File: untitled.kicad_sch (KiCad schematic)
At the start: 12 parts, among them J2 LED HDR, U1 74LVC2GU04

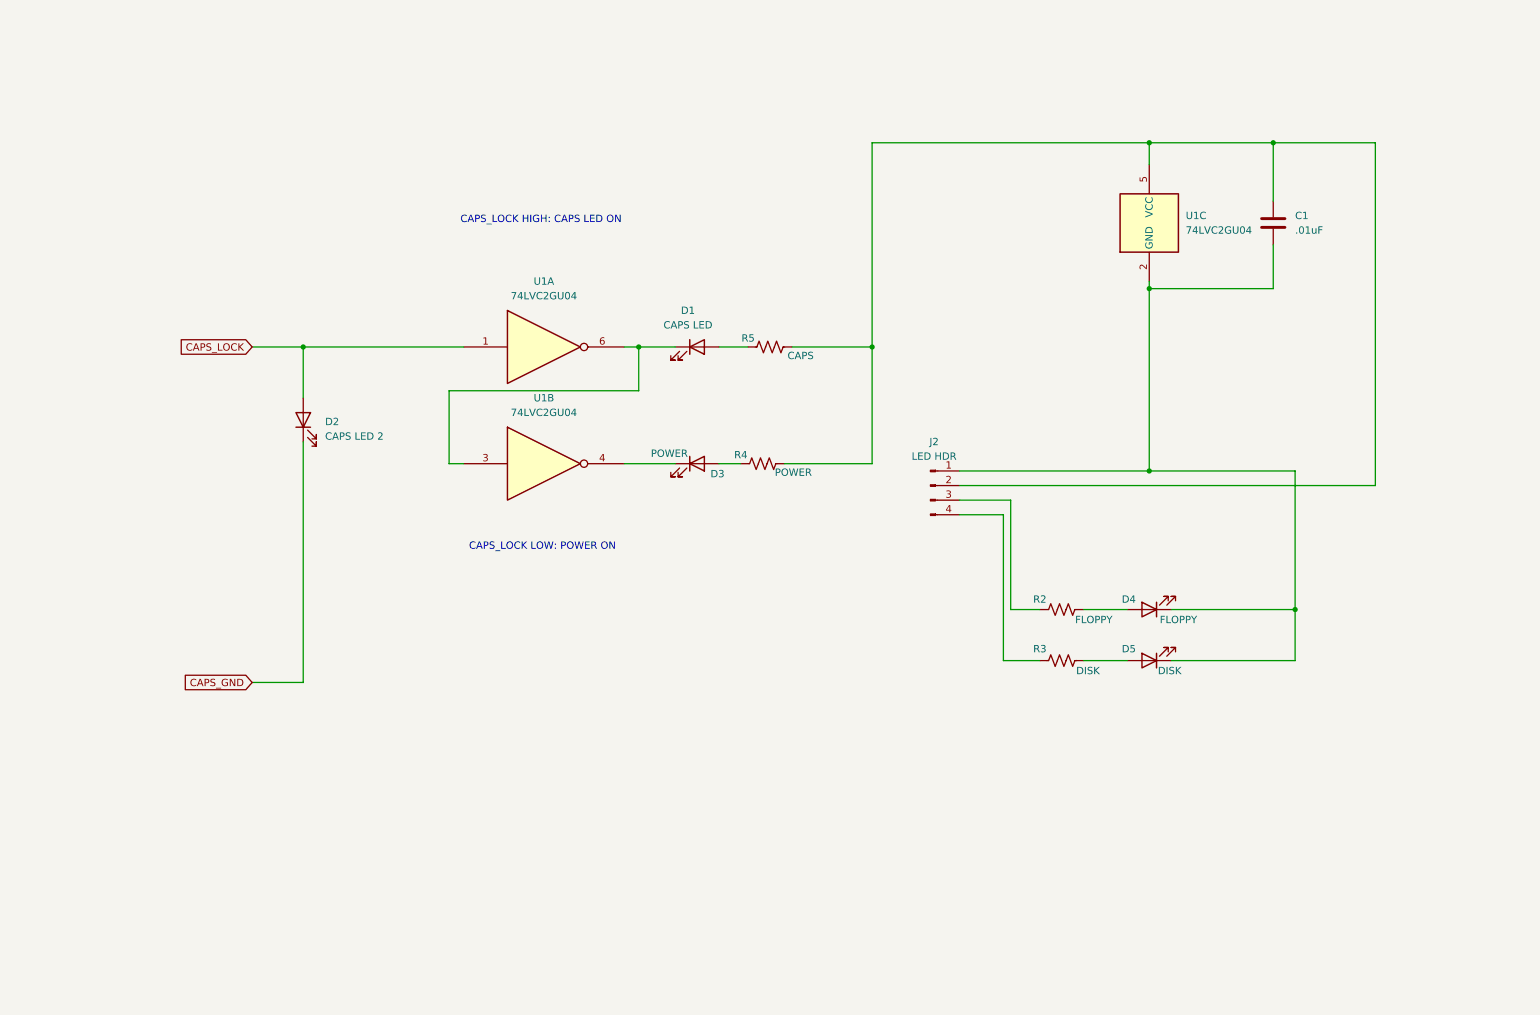
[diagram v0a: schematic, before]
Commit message: r2
smaller cutouts for stabilizers in PCB
removed unused mounting holes
board shorter by 2mm top/bottom to mount rails
add 0R option to use capslock under keycap only
silkscreen labels for switches
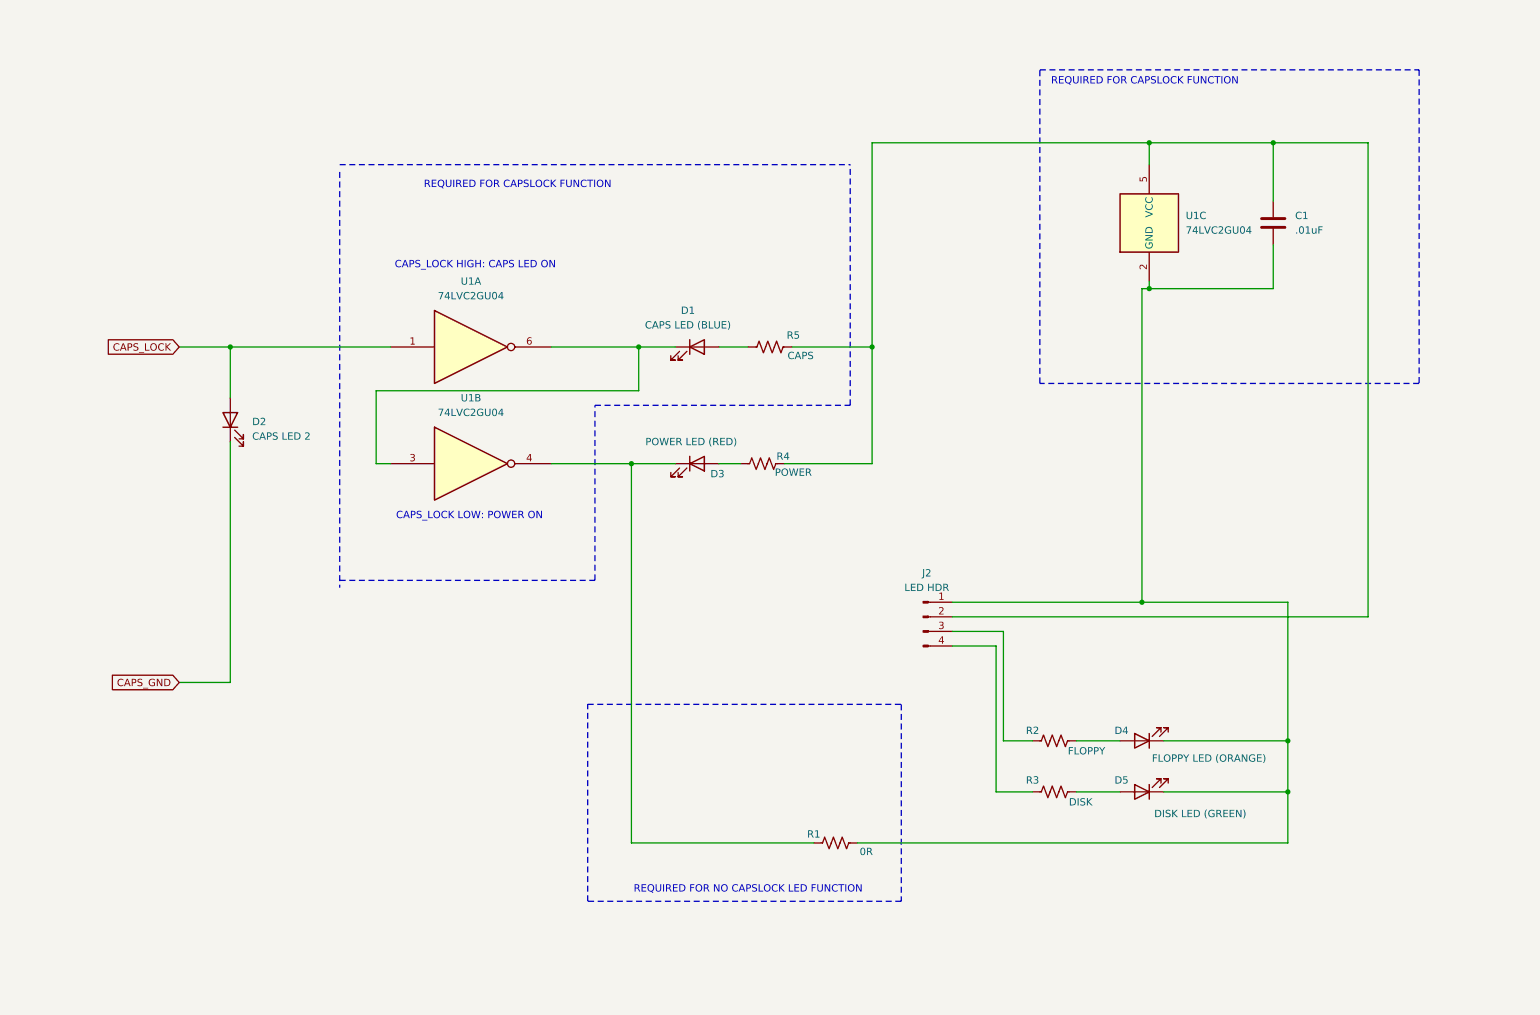
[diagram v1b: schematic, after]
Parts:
- added R1: 0R, Resistor_SMD:R_0805_2012Metric_Pad1.20x1.40mm_HandSolder, symbol Device:R_US
- D1: value CAPS LED -> CAPS LED (BLUE)
- D3: value POWER -> POWER LED (RED)
- D4: value FLOPPY -> FLOPPY LED (ORANGE)
- D5: value DISK -> DISK LED (GREEN)
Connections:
- net at C1.2, D4.1 (K), D5.1 (K)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: now also R1.2
- net at D3.1 (K), U1.4: now also R1.1
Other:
- note added: "REQUIRED FOR CAPSLOCK FUNCTION"
- note added: "REQUIRED FOR NO CAPSLOCK LED FUNCTION"
- moved on the sheet: D2, D4, D5, J2, R2, R3, U1A, U1B

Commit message: fab 9/7/24 KS-33 revised caps LED
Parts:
- D1: value CAPS LED (BLUE) -> POWER LED (RED)
- D3: value POWER LED (RED) -> CAPS LOCK (BLUE)
- R4: value POWER -> CAPS
- R5: value CAPS -> POWER
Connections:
- net CAPS_GND: now also U1.1
- net CAPS_LOCK renamed VCC
- net VCC: no longer U1.1
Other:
- moved on the sheet: D2
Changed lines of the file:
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@@
 	(paper "A4")
-	(junction
-		(at 53.34 73.66)
-		(diameter 0)
-		(color 0 0 0 0)
-	)
 	(junction
 		(at 124.46 73.66)
@@
 	)
 	(junction
+		(at 52.07 73.66)
+		(diameter 0)
+		(color 0 0 0 0)
+	)
+	(junction
 		(at 213.36 38.1)
 		(diameter 0)
@@
 	(wire
 		(pts
-			(xy 53.34 132.08) (xy 44.45 132.08)
-		)
-		(stroke
-			(width 0)
-			(type default)
-		)
-	)
-	(wire
-		(pts
-			(xy 53.34 73.66) (xy 53.34 82.55)
+			(xy 52.07 73.66) (xy 43.18 73.66)
+		)
+		(stroke
+			(width 0)
+			(type default)
+		)
+	)
+	(wire
+		(pts
+			(xy 52.07 41.91) (xy 52.07 50.8)
+		)
+		(stroke
+			(width 0)
+			(type default)
+		)
+	)
+	(wire
+		(pts
+			(xy 52.07 73.66) (xy 81.28 73.66)
 		)
 		(stroke
@@
 	(wire
 		(pts
-			(xy 53.34 73.66) (xy 81.28 73.66)
-		)
-		(stroke
-			(width 0)
-			(type default)
-		)
-	)
-	(wire
-		(pts
 			(xy 200.66 142.24) (xy 208.28 142.24)
 		)
@@
 	(wire
 		(pts
-			(xy 53.34 90.17) (xy 53.34 132.08)
+			(xy 52.07 58.42) (xy 52.07 73.66)
 		)
 		(stroke
@@
 	(wire
 		(pts
-			(xy 44.45 73.66) (xy 53.34 73.66)
+			(xy 43.18 41.91) (xy 52.07 41.91)
 		)
 		(stroke
@@
 		)
 	)
-	(global_label "CAPS_LOCK"
+	(global_label "VCC"
 		(shape input)
-		(at 44.45 73.66 180)
+		(at 43.18 41.91 180)
 		(fields_autoplaced yes)
 		(effects
@@
 		)
 		(property "Intersheetrefs" "${INTERSHEET_REFS}"
-			(at 30.7605 73.66 0)
+			(at 36.5662 41.91 0)
 			(effects
 				(font
@@
 	(global_label "CAPS_GND"
 		(shape input)
-		(at 44.45 132.08 180)
+		(at 43.18 73.66 180)
 		(fields_autoplaced yes)
 		(effects
@@
 		)
 		(property "Intersheetrefs" "${INTERSHEET_REFS}"
-			(at 31.7886 132.08 0)
+			(at 30.5186 73.66 0)
 			(effects
 				(font
@@
 	(symbol
 		(lib_id "Device:LED")
-		(at 53.34 86.36 90)
+		(at 52.07 54.61 90)
 		(unit 1)
 		(exclude_from_sim no)
@@
 		(fields_autoplaced yes)
 		(property "Reference" "D2"
-			(at 57.15 86.6774 90)
+			(at 55.88 54.9274 90)
 			(effects
 				(font
@@
 		)
 		(property "Value" "CAPS LED 2"
-			(at 57.15 89.2174 90)
+			(at 55.88 57.4674 90)
 			(effects
 				(font
@@
 		)
 		(property "Footprint" "LED_SMD:LED_0805_2012Metric"
-			(at 53.34 86.36 0)
+			(at 52.07 54.61 0)
 			(effects
 				(font
@@
 		)
 		(property "Datasheet" "~"
-			(at 53.34 86.36 0)
+			(at 52.07 54.61 0)
 			(effects
 				(font
@@
 		)
 		(property "Description" "Light emitting diode"
-			(at 53.34 86.36 0)
+			(at 52.07 54.61 0)
 			(effects
 				(font
@@
 			)
 		)
-		(property "Value" "CAPS"
+		(property "Value" "POWER"
 			(at 152.654 75.184 90)
 			(effects
@@
 			)
 		)
-		(property "Value" "POWER LED (RED)"
+		(property "Value" "CAPS LOCK (BLUE)"
 			(at 133.604 90.17 0)
 			(effects
@@
 			)
 		)
-		(property "Value" "POWER"
+		(property "Value" "CAPS"
 			(at 151.384 95.504 90)
 			(effects
@@
 			)
 		)
-		(property "Value" "CAPS LED (BLUE)"
+		(property "Value" "POWER LED (RED)"
 			(at 133.0325 69.85 0)
 			(effects

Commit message: All working with pullups and alt hdd led. New left plate.
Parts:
- removed J2: LED HDR, Connector_PinHeader_2.54mm:PinHeader_1x04_P2.54mm_Vertical, symbol Connector:Conn_01x04_Pin
- added C2: .01uF, Capacitor_SMD:C_0805_2012Metric_Pad1.18x1.45mm_HandSolder, symbol Device:C
- added D6: ALT HDD, LED_SMD:LED_0805_2012Metric, symbol Device:LED
- added J2: Conn_01x06_Pin, Connector_PinHeader_2.54mm:PinHeader_1x06_P2.54mm_Vertical, symbol Connector:Conn_01x06_Pin
- added R6, R8, R9: 10k, Resistor_SMD:R_0805_2012Metric_Pad1.20x1.40mm_HandSolder, symbol Device:R_US
- added R7: ~, Resistor_SMD:R_0805_2012Metric_Pad1.20x1.40mm_HandSolder, symbol Device:R_US
- added U2: 74LVC2GU04, Package_TO_SOT_SMD:SOT-23-6, symbol 74xGxx:74LVC2GU04
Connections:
- net CAPS_GND: now also R6.2
- net at R3.1: now also J2.4 (Pin_4)
- net at R2.1: now also J2.3 (Pin_3)
- net at C1.2, D4.1 (K), D5.1 (K)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: now also C2.2, J2.1 (Pin_1), R9.2, U2.2 (GND)
- net Input pullup: now reaches C1.1, R4.2, R5.2, U1.5 (VCC)
- net Input pullup: now also C2.1, J2.2 (Pin_2), R6.1, R7.2, R8.1, U2.5 (VCC)
- new net: D6.1 (K), U2.4
- new net: D6.2 (A), R7.1
- new net HDD LIGHT: J2.6 (Pin_6), R9.1, U2.3, U2.6
- new net /HDD_LIGHT: J2.5 (Pin_5), R8.2, U2.1
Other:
- note added: "CONNECT ONE ONLY!"
- moved on the sheet: C1, D1, D2, D3, D4, D5, R1, R2, R3, R4, R5, U1A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

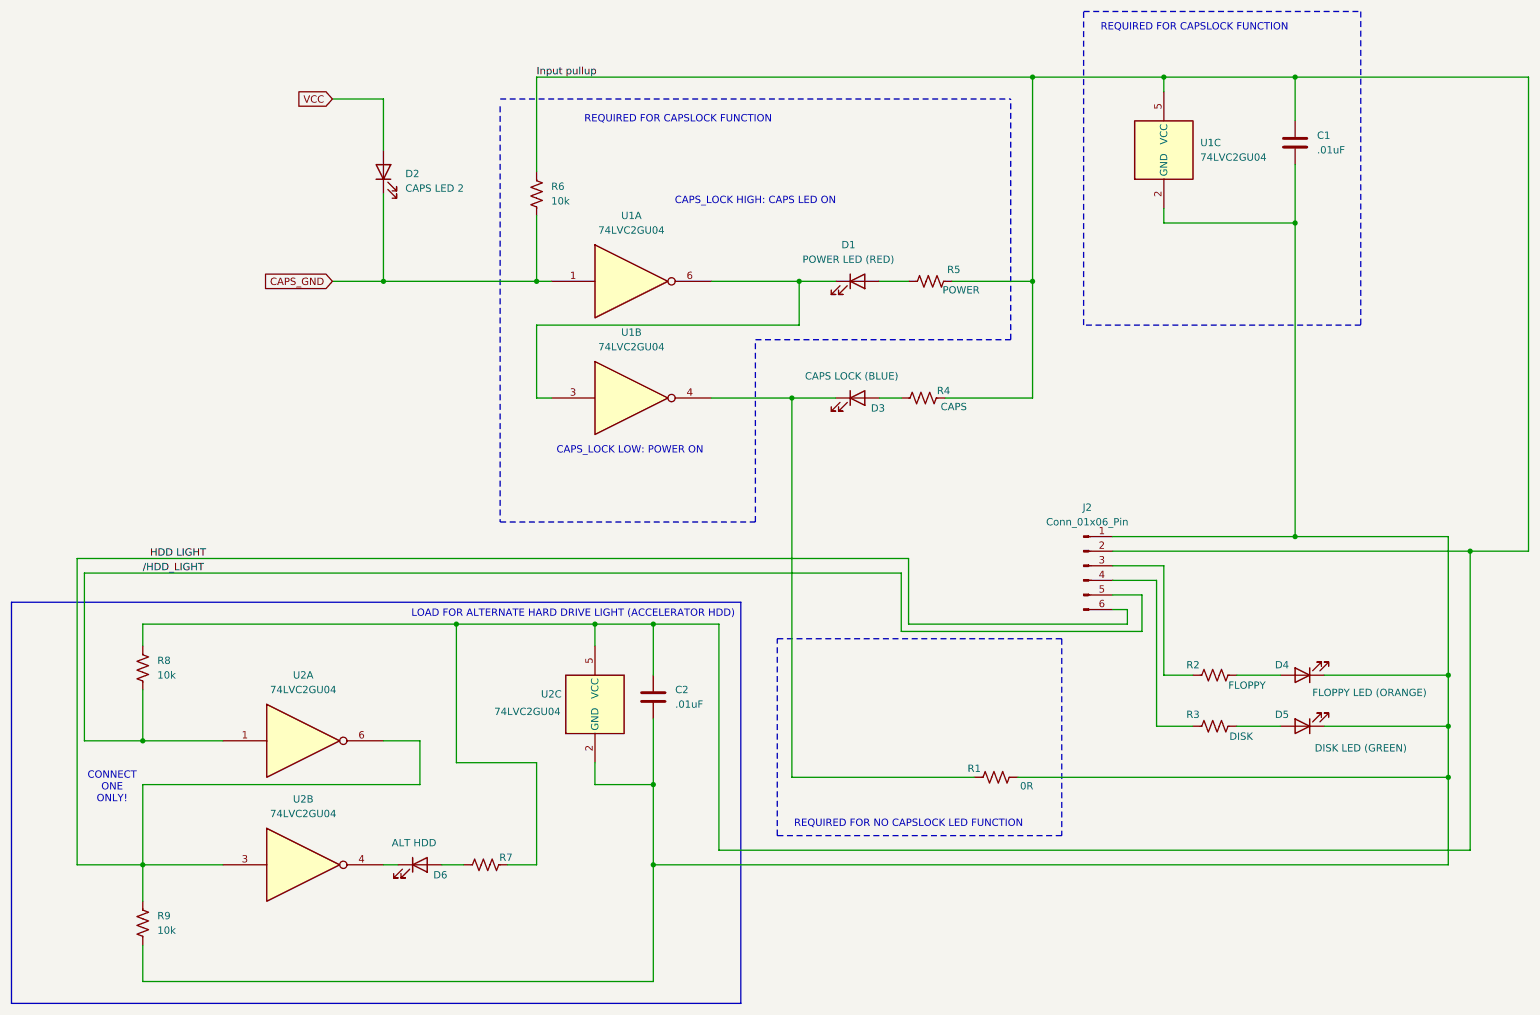
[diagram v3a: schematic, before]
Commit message: Fix up with pullup resistor for r3
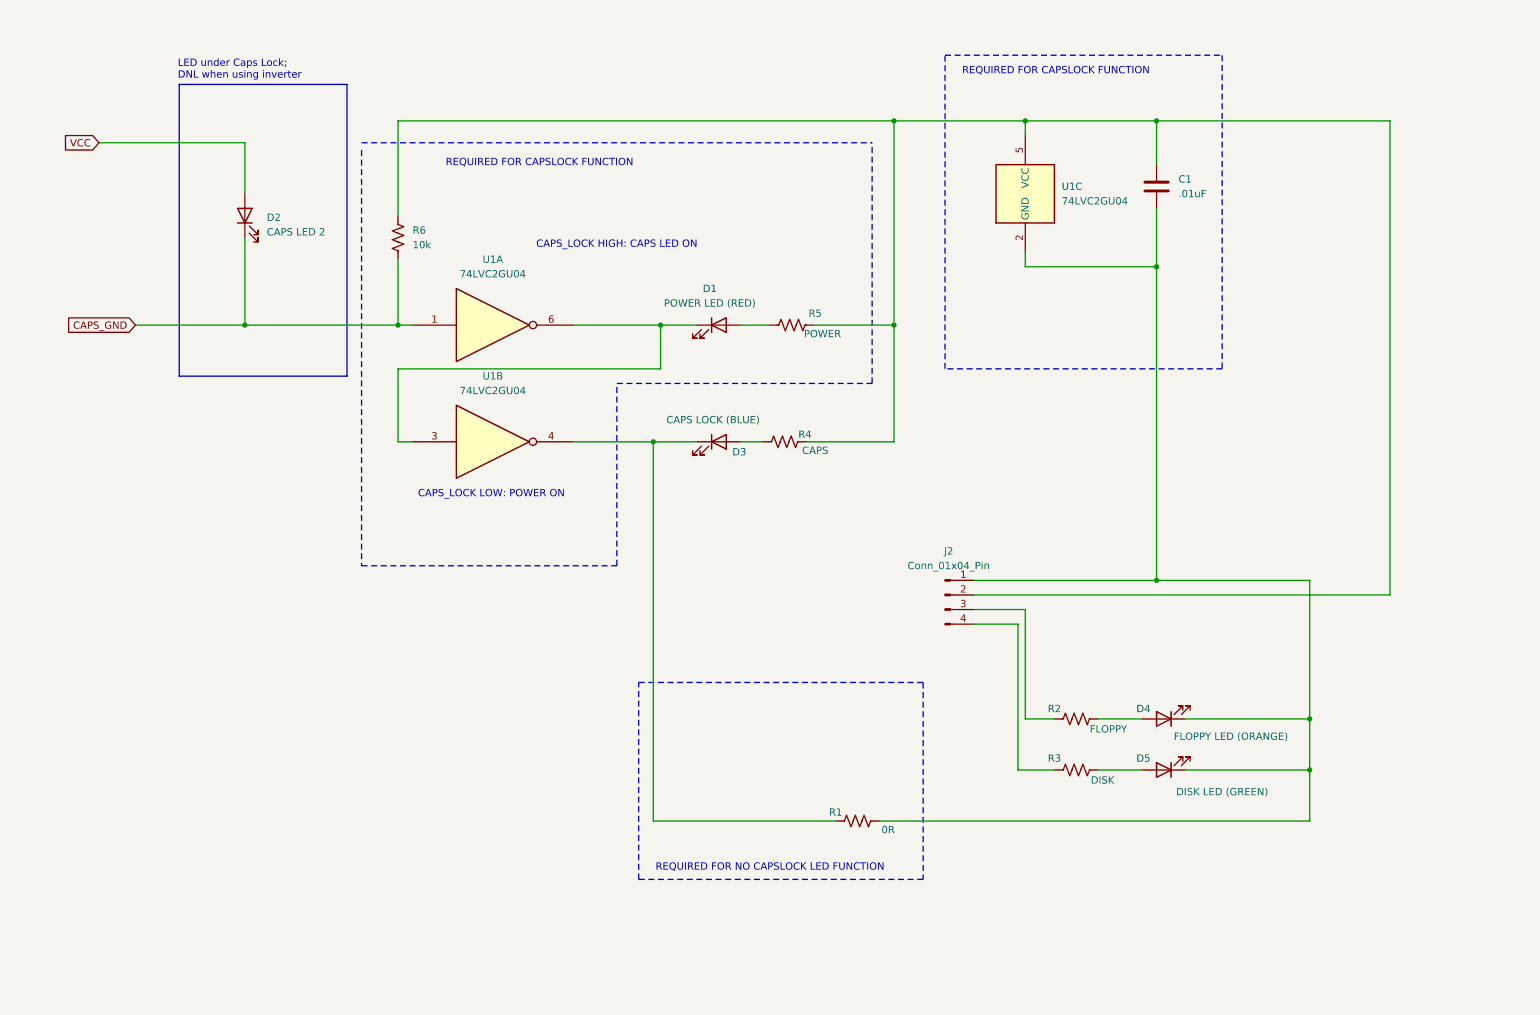
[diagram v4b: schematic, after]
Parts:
- removed C2: .01uF, Capacitor_SMD:C_0805_2012Metric_Pad1.18x1.45mm_HandSolder, symbol Device:C
- removed D6: ALT HDD, LED_SMD:LED_0805_2012Metric, symbol Device:LED
- removed J2: Conn_01x06_Pin, Connector_PinHeader_2.54mm:PinHeader_1x06_P2.54mm_Vertical, symbol Connector:Conn_01x06_Pin
- removed R7: ~, Resistor_SMD:R_0805_2012Metric_Pad1.20x1.40mm_HandSolder, symbol Device:R_US
- removed R8, R9: 10k, Resistor_SMD:R_0805_2012Metric_Pad1.20x1.40mm_HandSolder, symbol Device:R_US
- removed U2: 74LVC2GU04, Package_TO_SOT_SMD:SOT-23-6, symbol 74xGxx:74LVC2GU04
- added J2: Conn_01x04_Pin, Connector_PinHeader_2.54mm:PinHeader_1x04_P2.54mm_Vertical, symbol Connector:Conn_01x04_Pin
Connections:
- net at R3.1: now also J2.4 (Pin_4)
- net at C1.2, D4.1 (K), D5.1 (K)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: now also J2.1 (Pin_1)
- net at R2.1: now also J2.3 (Pin_3)
- net Input pullup: no longer names the net of C1.1, R4.2, R5.2, R6.1, U1.5 (VCC)
- net Input pullup: now also J2.2 (Pin_2)
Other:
- note added: "LED under Caps Lock; DNL when using inverter"
- note removed: "CONNECT ONE ONLY!"
- moved on the sheet: C1, D1, D2, D3, D4, D5, R1, R2, R3, R4, R5, R6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
